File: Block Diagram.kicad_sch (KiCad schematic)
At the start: 0 parts

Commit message: Finished 65% of schematics
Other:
- note removed: "+??V"
- note removed: "+A3V3"

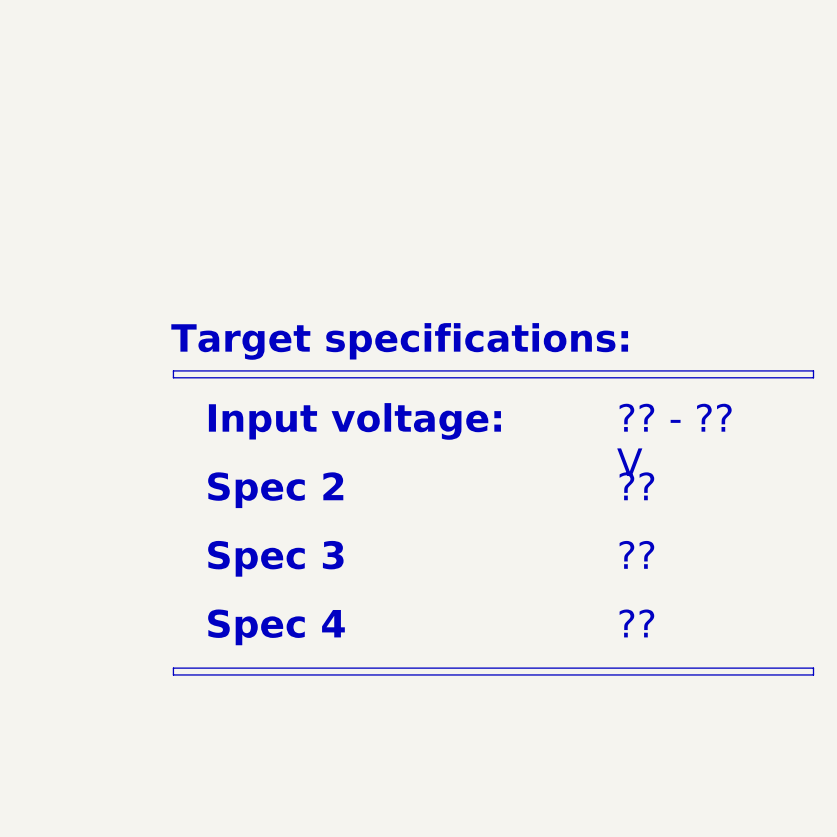
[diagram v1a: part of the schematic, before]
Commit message: Added footprints, images, almost finished all èages except for the MCU
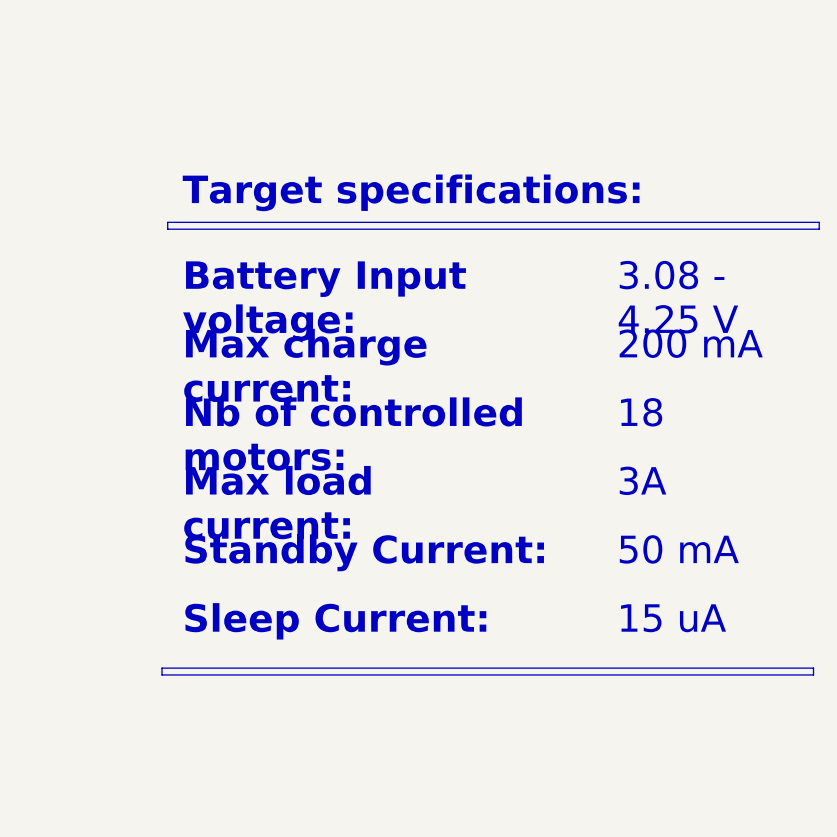
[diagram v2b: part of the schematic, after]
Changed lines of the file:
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@@
 	)
 	(rectangle
-		(start 331.47 237.49)
+		(start 330.2 237.49)
 		(end 402.59 238.252)
 		(stroke
@@
 	)
 	(rectangle
-		(start 331.47 204.47)
-		(end 402.59 205.232)
+		(start 330.835 187.96)
+		(end 403.225 188.722)
 		(stroke
 			(width 0)
@@
 		)
 	)
-	(text_box "Spec 3"
-		(exclude_from_sim no)
-		(at 332.74 220.98 0)
+	(text_box "Max load current:"
+		(exclude_from_sim no)
+		(at 330.2 212.725 0)
 		(size 41.91 7.62)
 		(margins 2.2859 2.2859 2.2859 2.2859)
 		(stroke
 			(width -0.0001)
-			(type default)
-		)
-		(fill
-			(type none)
-		)
-		(effects
-			(font
-				(face "Times New Roman")
-				(size 3.048 3.048)
-				(thickness 0.4572)
-				(bold yes)
-				(color 0 0 0 1)
-			)
-			(justify left top)
-		)
-	)
-	(text_box "Spec 2"
-		(exclude_from_sim no)
-		(at 332.74 213.36 0)
-		(size 43.18 7.62)
-		(margins 2.2859 2.2859 2.2859 2.2859)
-		(stroke
-			(width -0.0001)
-			(type default)
+			(type solid)
+		)
+		(fill
+			(type none)
+		)
+		(effects
+			(font
+				(face "Times New Roman")
+				(size 3.048 3.048)
+				(thickness 0.4572)
+				(bold yes)
+				(color 0 0 0 1)
+			)
+			(justify left top)
+		)
+	)
+	(text_box "Nb of controlled motors:"
+		(exclude_from_sim no)
+		(at 330.2 205.105 0)
+		(size 50.165 7.62)
+		(margins 2.2859 2.2859 2.2859 2.2859)
+		(stroke
+			(width -0.0001)
+			(type solid)
 		)
 		(fill
@@
 		)
 	)
-	(text_box "Input voltage:"
-		(exclude_from_sim no)
-		(at 332.74 205.74 0)
-		(size 41.91 7.62)
-		(margins 2.2859 2.2859 2.2859 2.2859)
-		(stroke
-			(width -0.0001)
-			(type default)
-		)
-		(fill
-			(type none)
-		)
-		(effects
-			(font
-				(face "Times New Roman")
-				(size 3.048 3.048)
-				(thickness 0.4572)
-				(bold yes)
-				(color 0 0 0 1)
-			)
-			(justify left top)
-		)
-	)
-	(text_box "??"
-		(exclude_from_sim no)
-		(at 378.46 228.6 0)
+	(text_box "Battery Input voltage:"
+		(exclude_from_sim no)
+		(at 330.2 189.865 0)
+		(size 47.625 7.62)
+		(margins 2.2859 2.2859 2.2859 2.2859)
+		(stroke
+			(width -0.0001)
+			(type solid)
+		)
+		(fill
+			(type none)
+		)
+		(effects
+			(font
+				(face "Times New Roman")
+				(size 3.048 3.048)
+				(thickness 0.4572)
+				(bold yes)
+				(color 0 0 0 1)
+			)
+			(justify left top)
+		)
+	)
+	(text_box "50 mA"
+		(exclude_from_sim no)
+		(at 378.46 220.345 0)
 		(size 24.13 7.62)
 		(margins 2.2859 2.2859 2.2859 2.2859)
 		(stroke
 			(width -0.0001)
-			(type default)
-		)
-		(fill
-			(type none)
-		)
-		(effects
-			(font
-				(face "Times New Roman")
-				(size 3.048 3.048)
-				(color 0 0 0 1)
-			)
-			(justify left top)
-		)
-	)
-	(text_box "??"
-		(exclude_from_sim no)
-		(at 378.46 213.36 0)
+			(type solid)
+		)
+		(fill
+			(type none)
+		)
+		(effects
+			(font
+				(face "Times New Roman")
+				(size 3.048 3.048)
+				(color 0 0 0 1)
+			)
+			(justify left top)
+		)
+	)
+	(text_box "18"
+		(exclude_from_sim no)
+		(at 378.46 205.105 0)
 		(size 24.13 7.62)
 		(margins 2.2859 2.2859 2.2859 2.2859)
 		(stroke
 			(width -0.0001)
-			(type default)
+			(type solid)
 		)
 		(fill
@@
 		)
 	)
+	(text_box "Max charge current:"
+		(exclude_from_sim no)
+		(at 330.2 197.485 0)
+		(size 47.625 7.62)
+		(margins 2.2859 2.2859 2.2859 2.2859)
+		(stroke
+			(width -0.0001)
+			(type solid)
+		)
+		(fill
+			(type none)
+		)
+		(effects
+			(font
+				(face "Times New Roman")
+				(size 3.048 3.048)
+				(thickness 0.4572)
+				(bold yes)
+				(color 0 0 0 1)
+			)
+			(justify left top)
+		)
+	)
 	(text_box "Target specifications:"
 		(exclude_from_sim no)
-		(at 328.93 196.85 0)
+		(at 330.2 180.34 0)
 		(size 73.66 7.62)
 		(margins 2.2859 2.2859 2.2859 2.2859)
@@
 		)
 	)
-	(text_box "??"
-		(exclude_from_sim no)
-		(at 378.46 220.98 0)
+	(text_box "3A"
+		(exclude_from_sim no)
+		(at 378.46 212.725 0)
 		(size 24.13 7.62)
 		(margins 2.2859 2.2859 2.2859 2.2859)
 		(stroke
 			(width -0.0001)
-			(type default)
-		)
-		(fill
-			(type none)
-		)
-		(effects
-			(font
-				(face "Times New Roman")
-				(size 3.048 3.048)
-				(color 0 0 0 1)
-			)
-			(justify left top)
-		)
-	)
-	(text_box "?? - ?? V"
-		(exclude_from_sim no)
-		(at 378.46 205.74 0)
+			(type solid)
+		)
+		(fill
+			(type none)
+		)
+		(effects
+			(font
+				(face "Times New Roman")
+				(size 3.048 3.048)
+				(color 0 0 0 1)
+			)
+			(justify left top)
+		)
+	)
+	(text_box "3.08 - 4.25 V"
+		(exclude_from_sim no)
+		(at 378.46 189.865 0)
+		(size 32.385 7.62)
+		(margins 2.2859 2.2859 2.2859 2.2859)
+		(stroke
+			(width -0.0001)
+			(type solid)
+		)
+		(fill
+			(type none)
+		)
+		(effects
+			(font
+				(face "Times New Roman")
+				(size 3.048 3.048)
+				(color 0 0 0 1)
+			)
+			(justify left top)
+		)
+	)
+	(text_box "15 uA"
+		(exclude_from_sim no)
+		(at 378.46 227.965 0)
 		(size 24.13 7.62)
 		(margins 2.2859 2.2859 2.2859 2.2859)
 		(stroke
 			(width -0.0001)
-			(type default)
-		)
-		(fill
-			(type none)
-		)
-		(effects
-			(font
-				(face "Times New Roman")
-				(size 3.048 3.048)
-				(color 0 0 0 1)
-			)
-			(justify left top)
-		)
-	)
-	(text_box "Spec 4"
-		(exclude_from_sim no)
-		(at 332.74 228.6 0)
-		(size 44.45 7.62)
-		(margins 2.2859 2.2859 2.2859 2.2859)
-		(stroke
-			(width -0.0001)
-			(type default)
-		)
-		(fill
+			(type solid)
+		)
+		(fill
+			(type none)
+		)
+		(effects
+			(font
+				(face "Times New Roman")
+				(size 3.048 3.048)
+				(color 0 0 0 1)
+			)
+			(justify left top)
+		)
+	)
+	(text_box "200 mA"
+		(exclude_from_sim no)
+		(at 378.46 197.485 0)
+		(size 32.385 7.62)
+		(margins 2.2859 2.2859 2.2859 2.2859)
+		(stroke
+			(width -0.0001)
+			(type solid)
+		)
+		(fill
+			(type none)
+		)
+		(effects
+			(font
+				(face "Times New Roman")
+				(size 3.048 3.048)
+				(color 0 0 0 1)
+			)
+			(justify left top)
+		)
+	)
+	(text_box "Sleep Current:"
+		(exclude_from_sim no)
+		(at 330.2 227.965 0)
+		(size 52.705 7.62)
+		(margins 2.2859 2.2859 2.2859 2.2859)
+		(stroke
+			(width -0.0001)
+			(type solid)
+		)
+		(fill
+			(type none)
+		)
+		(effects
+			(font
+				(face "Times New Roman")
+				(size 3.048 3.048)
+				(thickness 0.4572)
+				(bold yes)
+				(color 0 0 0 1)
+			)
+			(justify left top)
+		)
+	)
+	(text_box "Standby Current:"
+		(exclude_from_sim no)
+		(at 330.2 220.345 0)
+		(size 52.705 7.62)
+		(margins 2.2859 2.2859 2.2859 2.2859)
+		(stroke
+			(width -0.0001)
+			(type solid)
+		)
+		(fill

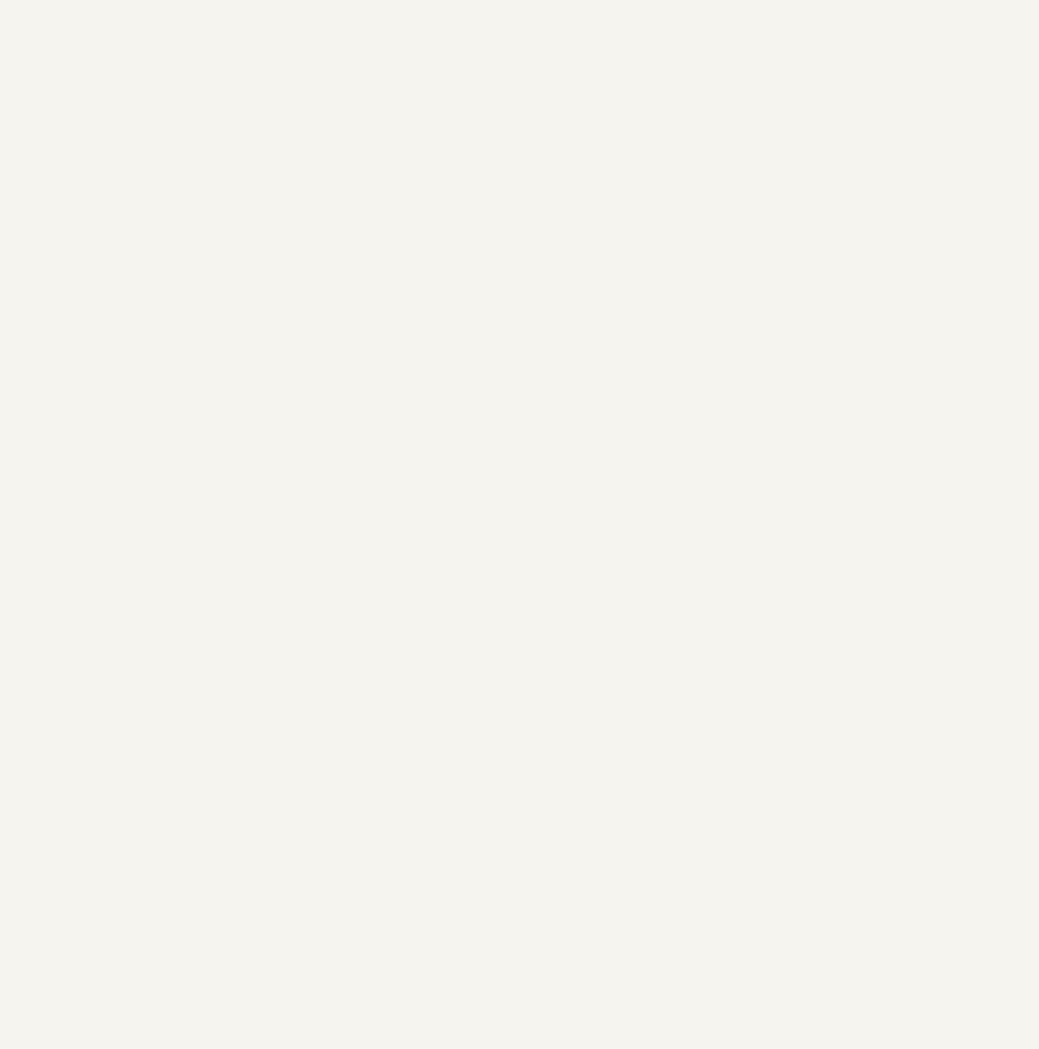
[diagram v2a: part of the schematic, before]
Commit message: Reviewed shematic, cleaned all DRC errors, chosed stackup, started layout
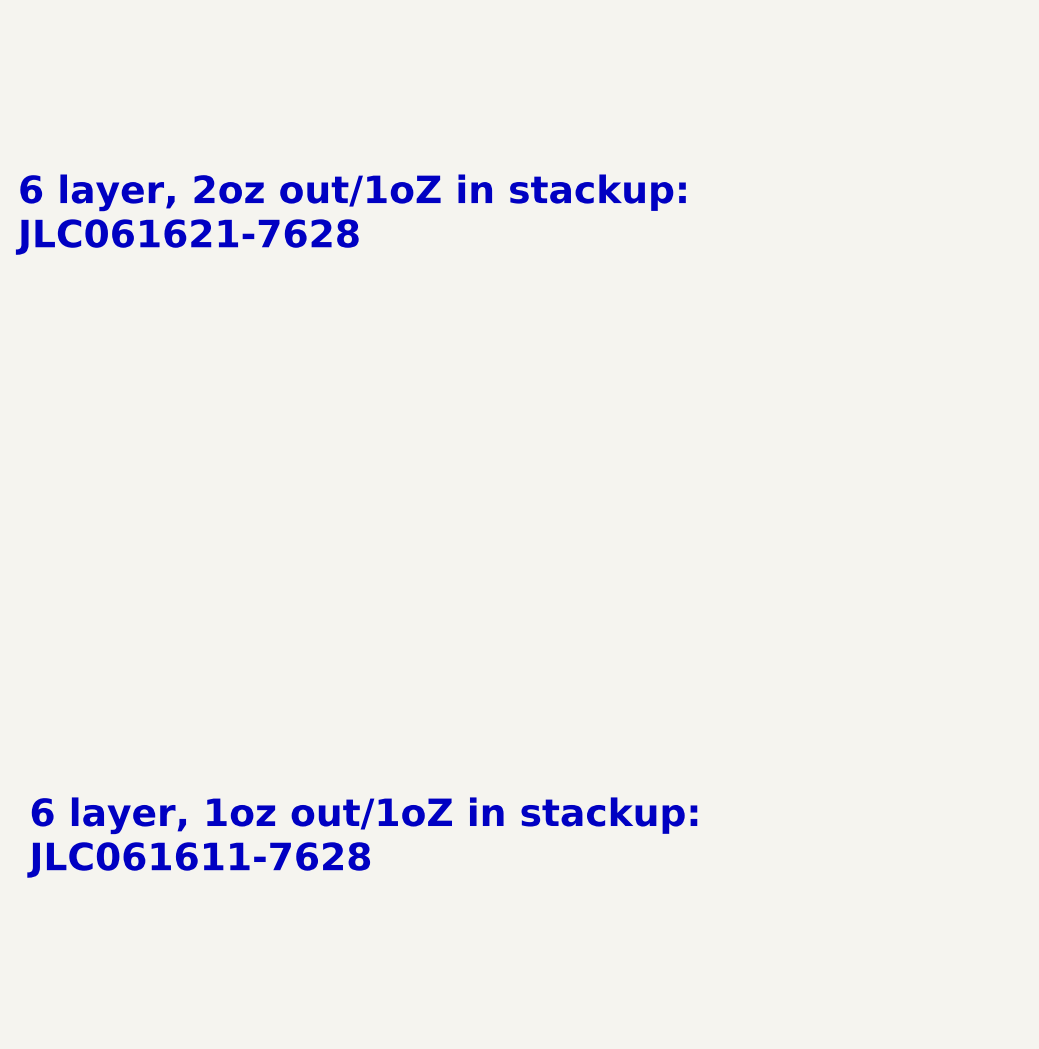
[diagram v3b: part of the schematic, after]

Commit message: Cleaned repo, cleaned and exported shematic, advanced rough layout
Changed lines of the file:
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@@
 	(title_block
 		(title "Block Diagram")
-		(date "2025-02-16")
+		(date "2025-04-05")
 		(rev "${REVISION}")
 		(company "${COMPANY}")
@@
 		)
 	)
-	(text_box "The purpose of this board is to be able to charge a battery and power the main load simultaneously from the same external power supply. The user have to be able to plug and unplug the power supply from the rover without shuting down/rebooting the load, requiring fast switching times. \n\nThe system will always try to use the external power supply as the primary power source for the rover, but will default to the battery if it is not availaible. "
-		(exclude_from_sim no)
-		(at 110.49 241.3 0)
-		(size 103.505 40.64)
-		(margins 2.405 2.405 2.405 2.405)
-		(stroke
-			(width 1)
-			(type solid)
-			(color 200 200 200 1)
-		)
-		(fill
-			(type none)
-		)
-		(effects
-			(font
-				(face "Times New Roman")
-				(size 2.54 2.54)
-				(thickness 0.4)
-				(bold yes)
-				(color 0 0 0 1)
-			)
-			(justify left top)
-		)
-	)
 	(text_box "Battery Input voltage:"
 		(exclude_from_sim no)
@@
 	(text_box "6 layer, 2oz out/1oZ in stackup: JLC061621-7628"
 		(exclude_from_sim no)
-		(at 29.845 135.255 0)
+		(at 34.29 235.585 0)
 		(size 95.885 7.62)
 		(margins 2.2859 2.2859 2.2859 2.2859)
@@
 	(text_box "6 layer, 1oz out/1oZ in stackup: JLC061611-7628"
 		(exclude_from_sim no)
-		(at 31.115 204.47 0)
+		(at 155.575 235.585 0)
 		(size 95.885 7.62)
 		(margins 2.2859 2.2859 2.2859 2.2859)
@@
 	)
 	(image
-		(at 62.23 238.76)
+		(at 201.93 262.89)
 		(scale 0.186283)
 		(data "iVBORw0KGgoAAAANSUhEUgAACpQAAATACAYAAAD0wzaiAAAKrmlDQ1BJQ0MgUHJvZmlsZQAASImV"
@@
 			"MTUpKSkpKHByb3BlcnR5ICJWYWx1ZSIgIjEwdSBYNVIgMTZWIihhdCAwIDEuNDMgMCkobGF5ZXIg"
 			"IkYuRmFiIiApKHV1aWQgIjBmYTFlODU1LWEwN2ItNGJkZC1hNGZhLTQxMDAxZGE1YzZkYiIpKGVm"
-			"ZmU="
+			"ZmUAAAAAAACAAAAAAAAAAAAAAAAAAAAAAGAFwW8BAAAArQAAAAAAAACuAAAAAAAAgAAAAAAAAAAA"
+			"AAAAAAAAAABQinkDAGAAAAgAAAAAAAAACgAAAAAAAIAAAAAAAAAAAAAAAAAAAAAAMAAAAAAAAAAI"
+			"AAAAAAAAAAoAAAAAAAABgGhuAgBgAAABAAAAAAAAADEAAAAxAAAAMgAAAAAAAAAKAAAAAAAAA5Bo"
+			"bgIAYAAAAwAAAAAAAAAxAAAAMQAAADIAAAAAAAAACgAAAAAAAAOgaG4CAGAAAAMAAAAAAAAAgIp5"
+			"AwBgAAALAAAAAAAAAAwAAAAAAACAAAAAAAAAAAAAAAAAAAAAAFAI7wwAYAAAGQAAAAAAAAAaAAAA"
+			"AAAAgAAAAAAAAAAAAAAAAAAAAACQC8FvAQAAANgAAAAAAAAA2gAAAAAAAIAAAAAAAAAAAAAAAAAA"
+			"AAAAsIp5AwBgAAAIAAAAAAAAAAoAAAAAAACAAAAAAAAAAAAAAAAAAAAAADAAAAAAAAAACAAAAAAA"
+			"AAAKAAAAAAAAAbBobgIAYAAAAQAAAAAAAAAxAAAAMwAAADIAAAAAAAAACgAAAAAAAAPAaG4CAGAA"
+			"AAMAAAAAAAAAMQAAADMAAAAyAAAAAAAAAAoAAAAAAAAD0GhuAgBgAAADAAAAAAAAAOCKeQMAYAAA"
+			"CwAAAAAAAAAMAAAAAAAAgAAAAAAAAAAAAAAAAAAAAAAAZ6cAAGAAAB4AAAAAAAAAIAAAAAAAAIAA"
+			"AAAAAAAAAAAAAAAAAAAAoBLBbwEAAADlAAAAAAAAAOYAAAAAAACAAAAAAAAAAAAAAAAAAAAAAAC8"
+			"BwAAYAAAFAAAAAAAAAAWAAAAAAAAgAAAAAAAAAAAAAAAAAAAAAAwAAAAAAAAABQAAAAAAAAAFgAA"
+			"AAAAAAHgaG4CAGAAAAEAAAAAAAAAMQAAADMAAAAyAAAAAAAAABYAAAAAAAAD8GhuAgBgAAADAAAA"
+			"AAAAADEAAAAzAAAAMgAAAAAAAAAWAAAAAAAAAwBpbgIAYAAAAwAAAAAAAAAQi3kDAGAAAAsAAAAA"
+			"AAAADAAAAAAAAIAAAAAAAAAAAAAAAAAAAAAAwAjvDABgAAAYAAAAAAAAABoAAAAAAACAAAAAAAAA"
+			"AAAAAAAAAAAAACAIwW8BAAAApQAAAAAAAACmAAAAAAAAgAAAAAAAAAAAAAAAAAAAAABAi3kDAGAA"
+			"AAgAAAAAAAAACgAAAAAAAIAAAAAAAAAAAAAAAAAAAAAAMAAAAAAAAAAIAAAAAAAAAAoAAAAAAAAB"
+			"EGluAgBgAAABAAAAAAAAADEAAAA0AAAANAAAAAAAAAAKAAAAAAAAAyBpbgIAYAAAAwAAAAAAAAAx"
+			"AAAAAAAAAAAAAAAAAAAAAAAAAAAAAAAAAAAAAAAAAAAAAAAAAAAAAAAAAAAAAAAAAAAAAAAAAAAA"
+			"AAAAAAAAAAAAAAAAAAAAAAAAAAAAAAAAAAAAAAAAAAAAAAAAAAAAAAAAAAAAAAAAAAAAAAAAAAAA"
+			"AAAAAAAAAAAAAAAAAAAAAAAAAAAAAAAAAAAAAAAAAAAAAAAAAAAAAAAAAAAAAAAAAAAAAAAAAAAA"
+			"AAAAAAAAAAAAAAAAAAAAAAAAAAAAAAAAAAAAAAAAAAAAAAAAAAAAAAAAAAAAAAAAAAAAAAAAAAAA"
+			"AAAAAAAAAAAAAAAAAAAAAAAAAAAAAAAAAAAAAAAAAAAAAAAAAAAAAAAAAAAAAAAAAAAAAAAAAAAA"
+			"AAAAAAAAAAAAAAAAAAAAAAAAAAAAAAAAAAAAAAAAAAAAAAAAAAAAAAAAAAAAAAAAAAAAAAAAAAAA"
+			"AAAAAAAAAAAAAAAAAAAAAAAAAAAAAAAAAAAAAAAAAAAAAAAAAAAAAAAAAAAAAAAAAAAAAAAAAAAA"
+			"AAAAAAAAAAAAAAAAAAAAAAAAAAAAAAAAAAAAAAAAAAAAAAAAAAAAAAAAAAAAAAAAAAAAAAAAAAAA"
+			"AAAAAAAAAAAAAAAAAAAAAAAAAAAAAAAAAAAAAAAAAAAAAAAAAAAAAAAAAAAAAAAAAAAAAAAAAAAA"
+			"AAAAAAAAAAAAAAAAAAAAAAAAAAAAAAAAAAAAAAAAAAAAAAAAAAAAAAAAAAAAAAAAAAAAAAAAAAAA"
+			"AAAAAAAAAAAAAAAAAAAAAAAAAAAAAAAAAAAAAAAAAAAAAAAAAAAAAAAAAAAAAAAAAAAAAAAAAAAA"
+			"AAAAAAAAAAAAAAAAAAAAAAAAAAAAAAAAAAAAAAAAAAAAAAAAAAAAAAAAAAAAAAAAAAAAAAAAAAAA"
+			"AAAAAAAAAAAAAAAAAAAAAAAAAAAAAAAAAAAAAAAAAAAAAAAAAAAAAAAAAAAAAAAAAAAAAAAAAAAA"
+			"AAAAAAAAAAAAAAAAAAAAAAAAAAAAAAAAAAAAAAAAAAAAAAAAAAAAAAAAAAAAAAAAAAAAAAAAAAAA"
+			"AAAAAAAAAAAAAAAAAAAAAAAAAAAAAAAAAAAAAAAAAAAAAAAAAAAAAAAAAAAAAAAAAAAAAAAAAAAA"
+			"AAAAAAAAAAAAAAAAAAAAAAAAAAAAAAAAAAAAAAAAAAAAAAAAAAAAAAAAAAAAAAAAAAAAAAAAAAAA"
+			"AAAAAAAAAAAAAAAAAAAAAAAAAAAAAAAAAAAAAAAAAAAAAAAAAAAAAAAAAAAAAAAAAAAAAAAAAAAA"
+			"AAAAAAAAAAAAAAAAAAAAAAAAAAAAAAAAAAAAAAAAAAAAAAAAAAAAAAAAAAAAAAAAAAAAAAAAAAAA"
+			"AA=="
 		)
 	)
 	(image
-		(at 95.25 170.18)
-		(scale 0.263589)
+		(at 81.915 262.89)
+		(scale 0.192442)
 		(data "iVBORw0KGgoAAAANSUhEUgAACpQAAASICAYAAAAXyL6jAAAKrmlDQ1BJQ0MgUHJvZmlsZQAASImV"
 			"lwdUk8kWx+f7vnQSCIQuJfQmSCeAlNBD781GSAKEEmMgKEVFZHEF14KICCgruiqi4FoAWQtiwYqA"
@@
 			"AAAAAAAAAAAAAAAAAAAAAAAAAAAAAAAAAAAAAAAAAAAAAAAAAAAAAAAAAAAAAAAAAAAAAAAAAAAA"
 			"AAAAAAAAAAAAAAAAAAAAAAAAAAAAAAAAAAAAAAAAAAAAAAAAAAAAAAAAAAAAAAAAAAAAAAAAAAAA"
-			"AAAAAAAAAAAAAAAAAAAAAAAAAAAAAAAAAAAAAAAAAAAAAAAAAAAAAAAAAAAAAAAAAAAAAAAAAAA="
+			"AAAAAAAAAAAAAAAAAAAAAAAAAAAAAAAAAAAAAAAAAAAAAAAAAAAAAAAAAAAAAAAAAAAAAAAAAAAA"
+			"AAAyAAAAKwAAAHgAAAB6AAAAMAAAADUAAABXAAAAZQAAADMAAABSAAAAZQAAAHcAAABZAAAATQAA"
+			"AFYAAAAvAAAAaAAAAHkAAABpAAAAOQAAAFUAAABSAAAARAAAAE4AAAB1AAAAdwAAAHMAAAA5AAAA"
+			"bgAAAGQAAAAvAAAAcgAAAEwAAABSAAAAMQAAAFIAAABXAAAATwAAAFYAAABOAAAANgAAAHYAAAA5"
+			"AAAATQAAAE0AAABDAAAAWQAAADgAAAB6AAAAVgAAAHMAAABrAAAANgAAAFIAAABwAAAAdQAAADIA"
+			"AABVAAAAOQAAAGYAAABsAAAAYgAAADcAAABwAAAAYgAAADkAAABYAAAAbwAAADkAAABjAAAAOAAA"
+			"AEwAAABFAAAAUQAAADUAAABkAAAAQwAAADUAAABwAAAAMwAAAHMAAAAzAAAAaAAAAE0AAABaAAAA"
+			"dgAAAHkAAAB1AAAANgAAADgAAAA3AAAAYQAAADAAAAA1AAAAUQAAAE8AAABuAAAAVAAAADQAAABD"
+			"AAAATAAAAFAAAAA1AAAANQAAAHIAAAAxAAAAeQAAADIAAABKAAAAWQAAAGkAAABLAAAATAAAADMA"
+			"AAB0AAAAOQAAAGwAAABGAAAAbQAAAGoAAABUAAAAWAAAAFcAAAB6AAAATQAAAGwAAABQAAAAQwAA"
+			"ACsAAABlAAAAZQAAAGMAAAA1AAAAWQAAAFoAAABQAAAAbQAAAHkAAABvAAAAVwAAAFcAAABLAAAA"
+			"SgAAAEoAAABjAAAAeQAAAFQAAABUAAAANAAAADkAAAAxAAAATQAAADEAAABJAAAAMgAAADIAAABh"
+			"AAAAaQAAAEgAAAAyAAAAMAAAADQAAABoAAAANwAAADkAAABkAAAAYwAAAE0AAAAzAAAAKwAAAGYA"
+			"AABNAAAASgAAAFAAAABsAAAAbAAAAGwAAAAvAAAAZQAAAGQAAABUAAAASgAAADYAAABiAAAAbAAA"
+			"AHcAAABYAAAAagAAAHYAAAA3AAAAVwAAADIAAAArAAAANgAAAHcAAABYAAAAawAAAGoAAABYAAAA"
+			"QwAAAGoAAABkAAAAeAAAADMAAAA3AAAAMAAAAG4AAAAxAAAARgAAAEIAAABRAAAAcQAAAGcAAABI"
+			"AAAAUgAAAGIAAABiAAAAZgAAAGUAAAAwAAAAbgAAAHoAAAA3AAAANwAAAGIAAABkAAAAdQAAAHgA"
+			"AAByAAAARQAAAGEAAABDAAAAVgAAADEAAABXAAAAVwAAADgAAAAxAAAANgAAAGkAAAArAAAAbgAA"
+			"AGcAAABEAAAARQAAAEMAAABhAAAAZQAAAGIAAAB6AAAAeAAAAGgAAAB0AAAAMwAAAGQAAAAvADFm"
+			"Slk0TkFRUVFPQzNnYnRvRWxQS1ZRQUFCQkJCQUFBRUVFRUFBQVFRUVFBQUJCS0lqUUh0TGRCelpD"
+			"Z0lJSUlBQUFnakVWb0E2UzJ4OTJUb0NDQ0NBQUFJSUlJQkFuSUNyZHhKUXlqY0NBUVFRU0FjQzdx"
+			"Wk5RR2s2dUZnY0lnSUlJSUFBQWdnZ2dBQUNDQ0NBQUFJSXBBc0IybHZTeFdYaUlCRkFBQUVFRU1q"
+			"MEF0UlpNdjFYQUFBRUVFQUFBUVFRUUNCRkJGeTlrNERTRk9GbUp3Z2dnRUJrQXU2bVRVQnBaSTZz"
+			"alFBQ0NDQ0FBQUlJSUlBQUFnZ2dnQUFDQ0RnQjJsdWNCSjhJSUlBQUFnZ2drSllGcUxPazVhdkRz"
+			"U0dBQUFJSUlJQUFBaGxId05VN0NTak5PTmVVTTBFQWdRd3M0RzdhQkpSbTRJdk1xU0dBQUFJSUlJ"
+			"QUFBZ2dnZ0FBQ0NDQ0FRSW9LME42U290enNEQUVFRUVBQUFRU1NLVUNkSlpsd3JJWUFBZ2dnZ0FB"
+			"Q0NDQ1FKQUZYN3lTZ05FbHNMSXdBQWdpa2pvQzdhUk5RbWpyKzdCVUJCQkJBQUFFRUVFQUFBUVFR"
+			"UUFBQkJES2VBTzB0R2UrYWNrWUlJSUFBQWdoa1JBSHFMQm54cW5KT0NDQ0FBQUlJSUlCQTJoTnc5"
+			"VTRDU3RQZXRlR0lFRUFBZ1hnQzdxWk5RR2s4R2lZZ2dBQUNDQ0NBQUFJSUlJQUFBZ2dnZ0FBQ3lS"
+			"S2d2U1ZaYkt5RUFBSUlJSUFBQWlrc1FKMGxoY0haSFFJSUlJQUFBZ2dna0VrRlhMMlRnTkpNK2dY"
+			"Z3RCRkFJSDBKdUpzMkFhWHA2N3B4dEFnZ2dBQUNDQ0NBQUFJSUlJQUFBZ2dna0hZRmFHOUp1OWVH"
+			"STBNQUFRUVFRQUNCL3dTb3MveG53UkFDQ0NDQUFBSUlJSUJBN0FSY3ZaT0EwdGdaczJVRUVFQWdh"
+			"Z0x1cGsxQWFkUkkyUkFDQ0NDQUFBSUlJSUFBQWdnZ2dBQUNDR1J5QWRwYk12a1hnTk5IQUFFRUVF"
+			"QWduUWhRWjBrbkY0ckRSQUFCQkJCQUFBRUUwcm1BcTNkbXFJRFN2LzcrUnphOXZsZis3Ly8rVDg0"
+			"LzkyeTVyL2dOVWJ0TWg0NzhLbS92L3RSdXIxekpJbkxPMmRtaXRtMDJoQUFDQ0NRbTRHN2FzUWdv"
+			"UFhYcWxEeTNkWS9vWjQ3c1owbjV1NHNtZGppWmZ2NlhCMytTcmU4Y2tPOSsvRmwrT1B5clpNOTJw"
+			"bHlXOXlLNUl2L0ZjbitKRzR3ai8wWkU4MHR5NUpmZjVZMTNQN0tidk9pQ2M2WFU3ZGVGM0x4Kw=="
 		)
 	)
